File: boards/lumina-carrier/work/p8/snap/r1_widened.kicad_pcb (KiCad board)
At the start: 4 copper layers, 100 x 80 mm, 116 parts, among them J1 LPJG0926HENL PoE+ RJ45 magjack, J2 1x6 2.54mm header (recovery), J3 DS1021-2x7SF11-B 2x7 male hea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, J4 DS1021-2x12SF11-B 2x12 male h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, SW1 SMD tactile switch, U1 TPS2378DDAR, U10 W5500, U20 SCT2A25STER, U21 TPS563201DDCR, U22 TPS16630PWPR, U30 ESP32-S3-WROOM-1-N8, Y10 25MHz 18pF CL crystal

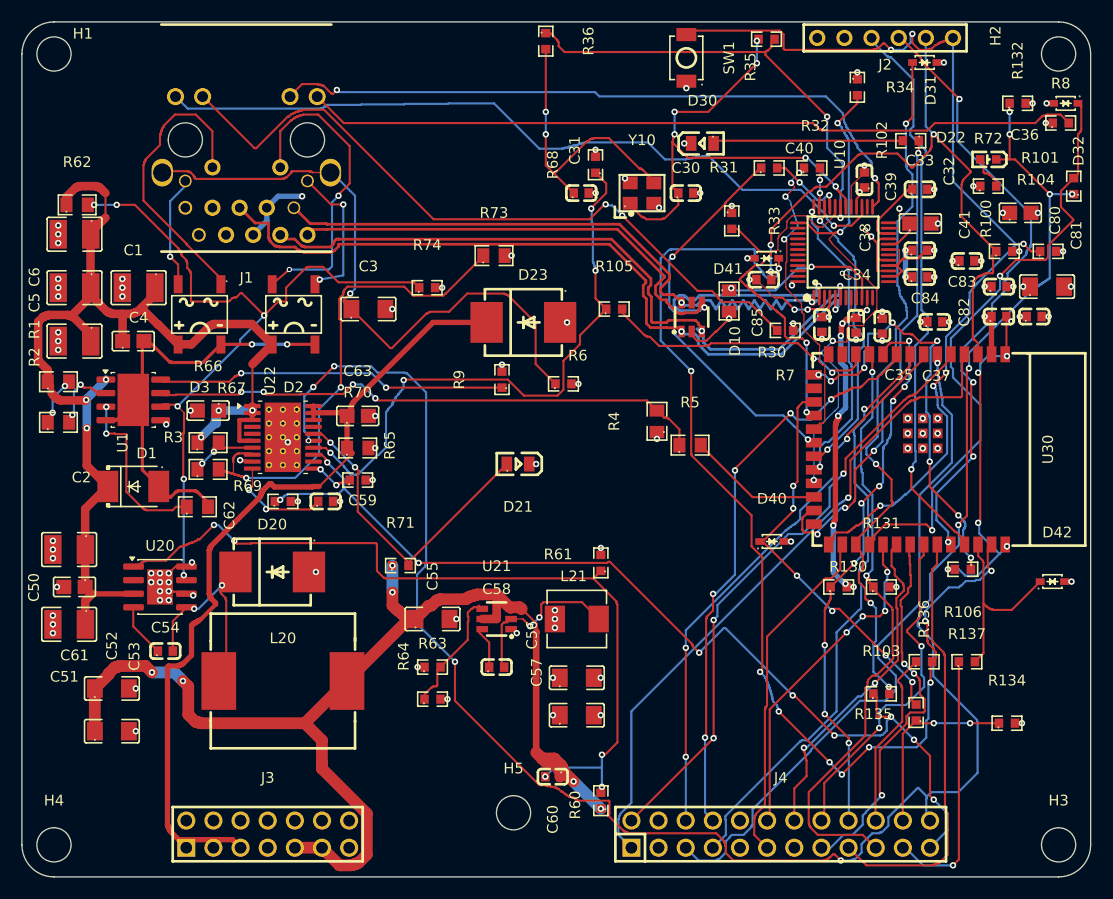
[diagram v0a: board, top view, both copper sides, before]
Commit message: ai-ee lumina-carrier: P8 fix loop 220->120 errors, diffpair PASS, drc_routed held 0/0
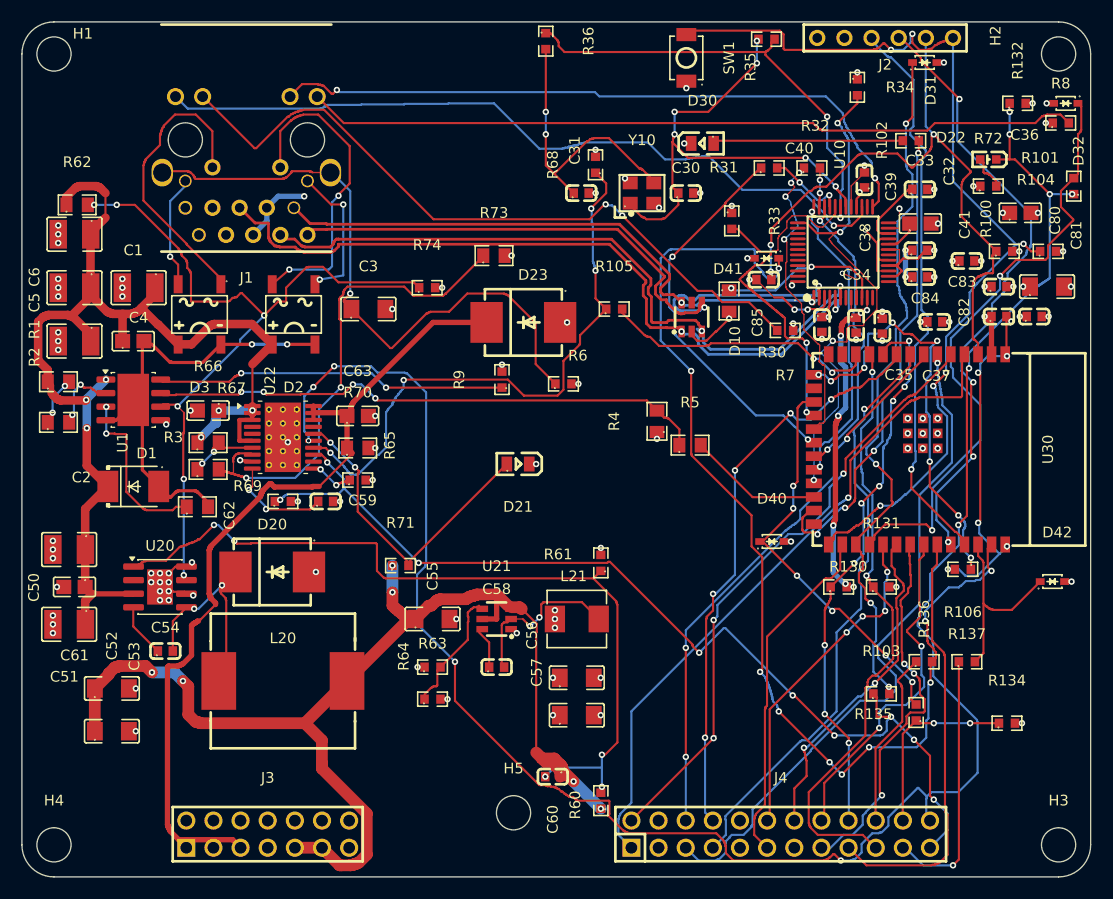
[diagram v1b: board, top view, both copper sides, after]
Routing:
- net /ETH_TXN: track 62.4 -> 55.9 mm
- net +3V3: track 62.0 -> 62.2 mm, vias 40 -> 38
